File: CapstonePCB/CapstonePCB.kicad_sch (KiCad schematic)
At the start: 29 parts, among them J1 Conn_02x40_Counter_Clockwise, J2 Barrel_Jack, U1 NUCLEO64-F411RE, U2 LP-MSPM0G3507, U3 STSPIN220, U4 74HC14, U5 LM7805_TO220, U6 TLV1117-33, U8 APDS-9306

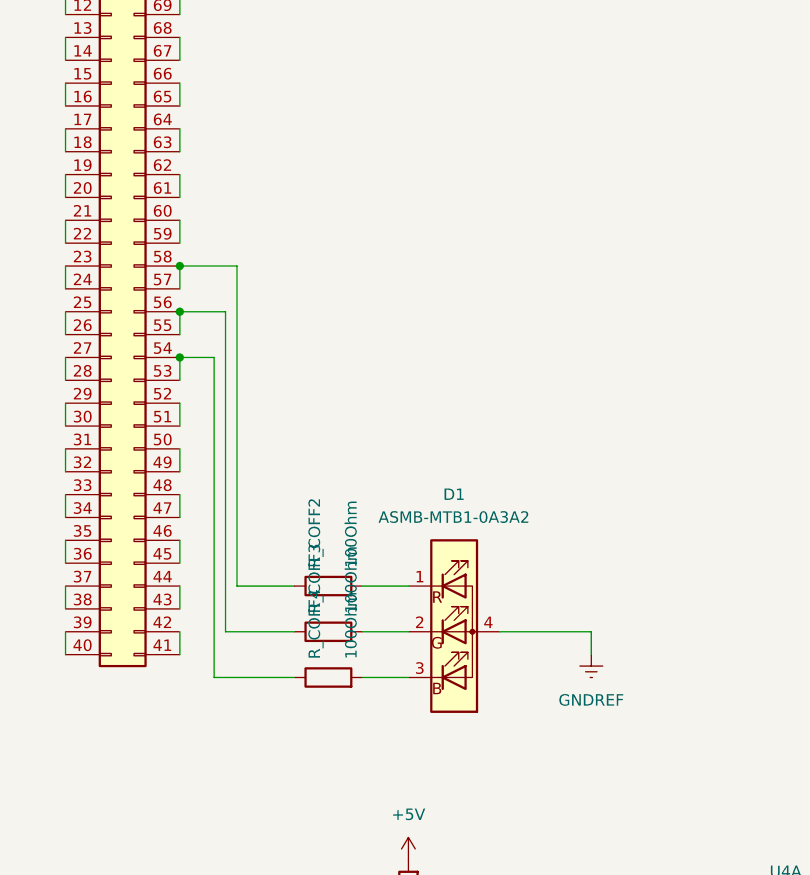
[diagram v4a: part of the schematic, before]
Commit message: Added footprints to motor driver circuit components
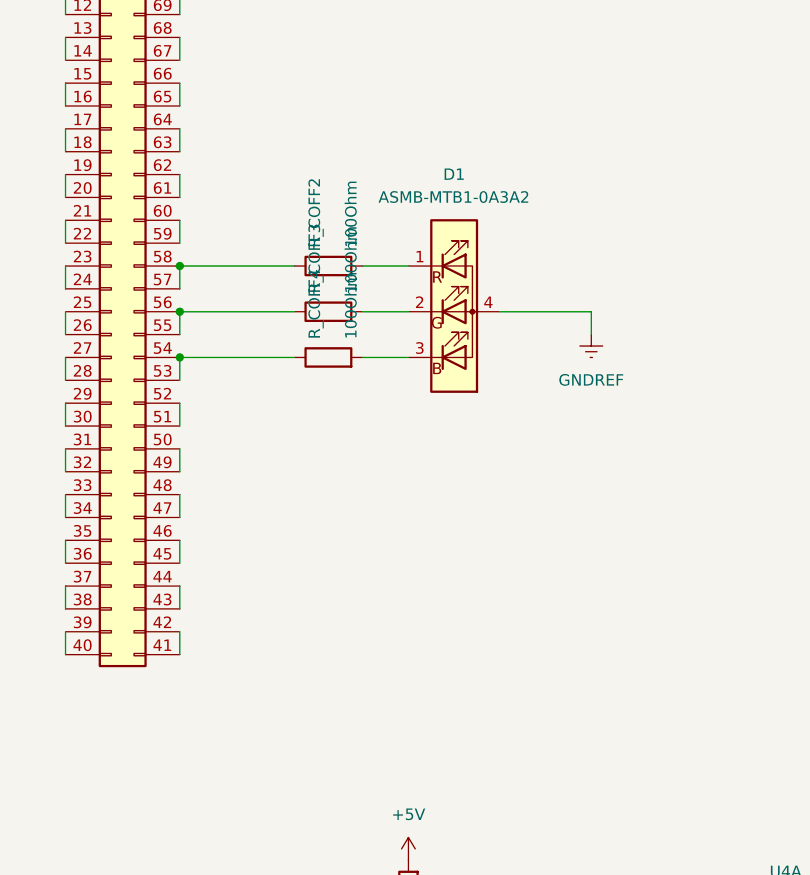
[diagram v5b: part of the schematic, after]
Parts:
- C_EN1, C_EN2, C_SPOIL1, C_STBY1, C_s1: footprint (none) -> Capacitor_SMD:C_0201_0603Metric
- R_COFF1, R_EN1, R_OFF1, R_SNSA1, R_SNSB1, R_STBY1: footprint (none) -> Resistor_SMD:R_0201_0603Metric
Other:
- moved on the sheet: D1, R_COFF2, R_COFF3, R_COFF4
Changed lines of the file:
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@@
 	(wire
 		(pts
-			(xy 160.02 115.57) (xy 152.4 115.57)
-		)
-		(stroke
-			(width 0)
-			(type default)
-		)
-	)
-	(wire
-		(pts
 			(xy 80.01 20.32) (xy 88.9 20.32)
 		)
@@
 	(wire
 		(pts
-			(xy 160.02 120.65) (xy 151.13 120.65)
-		)
-		(stroke
-			(width 0)
-			(type default)
-		)
-	)
-	(wire
-		(pts
 			(xy 134.62 85.09) (xy 134.62 87.63)
 		)
@@
 	(wire
 		(pts
-			(xy 193.04 115.57) (xy 193.04 118.11)
+			(xy 193.04 80.01) (xy 193.04 82.55)
 		)
 		(stroke
@@
 	(wire
 		(pts
-			(xy 153.67 110.49) (xy 153.67 74.93)
-		)
-		(stroke
-			(width 0)
-			(type default)
-		)
-	)
-	(wire
-		(pts
 			(xy 391.16 25.4) (xy 369.57 25.4)
 		)
@@
 	(wire
 		(pts
-			(xy 152.4 80.01) (xy 147.32 80.01)
+			(xy 147.32 80.01) (xy 160.02 80.01)
 		)
 		(stroke
@@
 	(wire
 		(pts
-			(xy 151.13 85.09) (xy 147.32 85.09)
+			(xy 147.32 85.09) (xy 160.02 85.09)
 		)
 		(stroke
@@
 	(wire
 		(pts
+			(xy 326.39 78.74) (xy 326.39 82.55)
+		)
+		(stroke
+			(width 0)
+			(type default)
+		)
+	)
+	(wire
+		(pts
 			(xy 318.77 50.8) (xy 318.77 53.34)
 		)
@@
 	(wire
 		(pts
-			(xy 167.64 110.49) (xy 172.72 110.49)
-		)
-		(stroke
-			(width 0)
-			(type default)
-		)
-	)
-	(wire
-		(pts
-			(xy 151.13 120.65) (xy 151.13 85.09)
+			(xy 167.64 74.93) (xy 172.72 74.93)
 		)
 		(stroke
@@
 	(wire
 		(pts
-			(xy 153.67 110.49) (xy 160.02 110.49)
-		)
-		(stroke
-			(width 0)
-			(type default)
-		)
-	)
-	(wire
-		(pts
 			(xy 104.14 20.32) (xy 107.95 20.32)
 		)
@@
 	(wire
 		(pts
-			(xy 152.4 115.57) (xy 152.4 80.01)
-		)
-		(stroke
-			(width 0)
-			(type default)
-		)
-	)
-	(wire
-		(pts
-			(xy 167.64 120.65) (xy 172.72 120.65)
+			(xy 167.64 85.09) (xy 172.72 85.09)
 		)
 		(stroke
@@
 	(wire
 		(pts
-			(xy 153.67 74.93) (xy 147.32 74.93)
+			(xy 147.32 74.93) (xy 160.02 74.93)
 		)
 		(stroke
@@
 	(wire
 		(pts
-			(xy 326.39 78.74) (xy 326.39 82.55)
-		)
-		(stroke
-			(width 0)
-			(type default)
-		)
-	)
-	(wire
-		(pts
 			(xy 134.62 39.37) (xy 134.62 41.91)
 		)
@@
 	(wire
 		(pts
-			(xy 182.88 115.57) (xy 193.04 115.57)
+			(xy 182.88 80.01) (xy 193.04 80.01)
 		)
 		(stroke
@@
 	(wire
 		(pts
-			(xy 167.64 115.57) (xy 172.72 115.57)
+			(xy 167.64 80.01) (xy 172.72 80.01)
 		)
 		(stroke
@@
 			)
 		)
-		(property "Footprint" ""
+		(property "Footprint" "Capacitor_SMD:C_0201_0603Metric"
 			(at 391.16 29.21 0)
 			(effects
@@
 	(symbol
 		(lib_id "Device:R")
-		(at 163.83 115.57 90)
+		(at 163.83 80.01 90)
 		(unit 1)
 		(exclude_from_sim no)
@@
 		(dnp no)
 		(property "Reference" "R_COFF3"
-			(at 162.306 113.538 0)
+			(at 162.306 77.978 0)
 			(effects
 				(font
@@
 		)
 		(property "Value" "100Ohm"
-			(at 166.37 113.538 0)
+			(at 166.37 77.978 0)
 			(effects
 				(font
@@
 		)
 		(property "Footprint" "Resistor_SMD:R_0201_0603Metric"
-			(at 163.83 117.348 90)
+			(at 163.83 81.788 90)
 			(effects
 				(font
@@
 		)
 		(property "Datasheet" "~"
-			(at 163.83 115.57 0)
+			(at 163.83 80.01 0)
 			(effects
 				(font
@@
 		)
 		(property "Description" "Resistor"
-			(at 163.83 115.57 0)
+			(at 163.83 80.01 0)
 			(effects
 				(font
@@
 			)
 		)
-		(property "Footprint" ""
+		(property "Footprint" "Resistor_SMD:R_0201_0603Metric"
 			(at 316.992 46.99 90)
 			(effects
@@
 			)
 		)
-		(property "Footprint" ""
+		(property "Footprint" "Capacitor_SMD:C_0201_0603Metric"
 			(at 326.39 85.09 0)
 			(effects
@@
 	(symbol
 		(lib_id "Device:R")
-		(at 163.83 110.49 90)
+		(at 163.83 74.93 90)
 		(unit 1)
 		(exclude_from_sim no)
@@
 		(dnp no)
 		(property "Reference" "R_COFF2"
-			(at 162.306 108.458 0)
+			(at 162.306 72.898 0)
 			(effects
 				(font
@@
 		)
 		(property "Value" "100Ohm"
-			(at 166.37 108.458 0)
+			(at 166.37 72.898 0)
 			(effects
 				(font
@@
 		)
 		(property "Footprint" "Resistor_SMD:R_0201_0603Metric"
-			(at 163.83 112.268 90)
+			(at 163.83 76.708 90)
 			(effects
 				(font
@@
 		)
 		(property "Datasheet" "~"
-			(at 163.83 110.49 0)
+			(at 163.83 74.93 0)
 			(effects
 				(font
@@
 		)
 		(property "Description" "Resistor"
-			(at 163.83 110.49 0)
+			(at 163.83 74.93 0)
 			(effects
 				(font
@@
 			)
 		)
-		(property "Footprint" ""
+		(property "Footprint" "Capacitor_SMD:C_0201_0603Metric"
 			(at 318.77 60.96 0)
 			(effects
@@
 	(symbol
 		(lib_id "power:GNDREF")
-		(at 193.04 118.11 0)
+		(at 193.04 82.55 0)
 		(unit 1)
 		(exclude_from_sim no)
@@
 		(fields_autoplaced yes)
 		(property "Reference" "#PWR023"
-			(at 193.04 124.46 0)
+			(at 193.04 88.9 0)
 			(effects
 				(font
@@
 		)
 		(property "Value" "GNDREF"
-			(at 193.04 123.19 0)
+			(at 193.04 87.63 0)
 			(effects
 				(font
@@
 		)
 		(property "Footprint" ""
-			(at 193.04 118.11 0)
+			(at 193.04 82.55 0)
 			(effects
 				(font
@@
 		)
 		(property "Datasheet" ""
-			(at 193.04 118.11 0)
+			(at 193.04 82.55 0)
 			(effects
 				(font
@@
 		)
 		(property "Description" ""
-			(at 193.04 118.11 0)
+			(at 193.04 82.55 0)
 			(effects
 				(font
@@
 			)
 		)
-		(property "Footprint" ""
+		(property "Footprint" "Resistor_SMD:R_0201_0603Metric"
 			(at 334.772 74.93 90)
 			(effects
@@
 			)
 		)
-		(property "Footprint" ""
+		(property "Footprint" "Resistor_SMD:R_0201_0603Metric"
 			(at 365.252 60.96 90)
 			(effects
@@
 			)
 		)
-		(property "Footprint" ""
+		(property "Footprint" "Resistor_SMD:R_0201_0603Metric"
 			(at 301.752 48.26 90)
 			(effects
@@
 			)
 		)
-		(property "Footprint" ""
+		(property "Footprint" "Resistor_SMD:R_0201_0603Metric"
 			(at 324.612 74.93 90)
 			(effects
@@
 			)
 		)
-		(property "Footprint" ""
+		(property "Footprint" "Capacitor_SMD:C_0201_0603Metric"
 			(at 369.57 29.21 0)
 			(effects
@@
 			)
 		)
-		(property "Footprint" ""
+		(property "Footprint" "Capacitor_SMD:C_0201_0603Metric"
 			(at 303.53 58.42 0)
 			(effects
@@
 			)
 		)
-		(property "Footprint" ""
+		(property "Footprint" "Resistor_SMD:R_0201_0603Metric"
 			(at 369.062 48.26 90)
 			(effects
@@
 	(symbol
 		(lib_id "LED:ASMB-MTB1-0A3A2")
-		(at 177.8 115.57 0)
+		(at 177.8 80.01 0)
 		(unit 1)
 		(exclude_from_sim no)
@@
 		(fields_autoplaced yes)
 		(property "Reference" "D1"
-			(at 177.8 100.33 0)
+			(at 177.8 64.77 0)
 			(effects
 				(font
@@
 		)
 		(property "Value" "ASMB-MTB1-0A3A2"
-			(at 177.8 102.87 0)
+			(at 177.8 67.31 0)
 			(effects
 				(font
@@
 		)
 		(property "Footprint" "LED_SMD:LED_Avago_PLCC4_3.2x2.8mm_CW"
-			(at 177.8 100.33 0)
+			(at 177.8 64.77 0)
 			(effects
 				(font
@@
 		)
 		(property "Datasheet" "https://docs.broadcom.com/docs/AV02-4194EN"
-			(at 177.8 127 0)
+			(at 177.8 91.44 0)
 			(effects
 				(font
@@
 		)
 		(property "Description" "Tricolor Black Surface LED, Common Anode Pin 4, PLCC-4"
-			(at 177.8 115.57 0)
+			(at 177.8 80.01 0)
 			(effects
 				(font
@@
 	(symbol
 		(lib_id "Device:R")
-		(at 163.83 120.65 90)
+		(at 163.83 85.09 90)
 		(unit 1)
 		(exclude_from_sim no)
@@
 		(dnp no)
 		(property "Reference" "R_COFF4"
-			(at 162.306 118.618 0)
+			(at 162.306 83.058 0)
 			(effects
 				(font
@@
 		)
 		(property "Value" "100Ohm"
-			(at 166.37 118.618 0)
+			(at 166.37 83.058 0)
 			(effects
 				(font
@@
 		)
 		(property "Footprint" "Resistor_SMD:R_0201_0603Metric"
-			(at 163.83 122.428 90)
+			(at 163.83 86.868 90)
 			(effects
 				(font
@@
 		)
 		(property "Datasheet" "~"
-			(at 163.83 120.65 0)
+			(at 163.83 85.09 0)
 			(effects
 				(font
@@
 		)
 		(property "Description" "Resistor"
-			(at 163.83 120.65 0)
+			(at 163.83 85.09 0)
 			(effects
 				(font

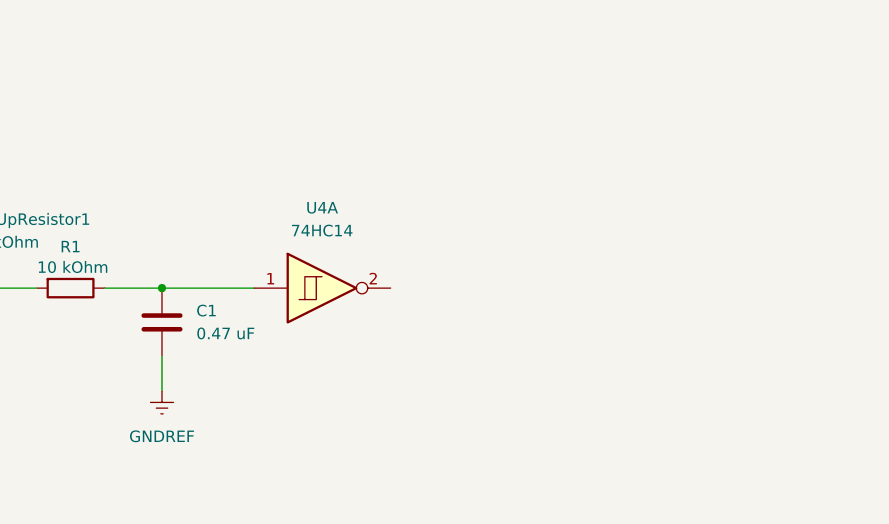
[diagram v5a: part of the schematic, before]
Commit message: Added in component for 8 bit schmitt trigger for button debouncing
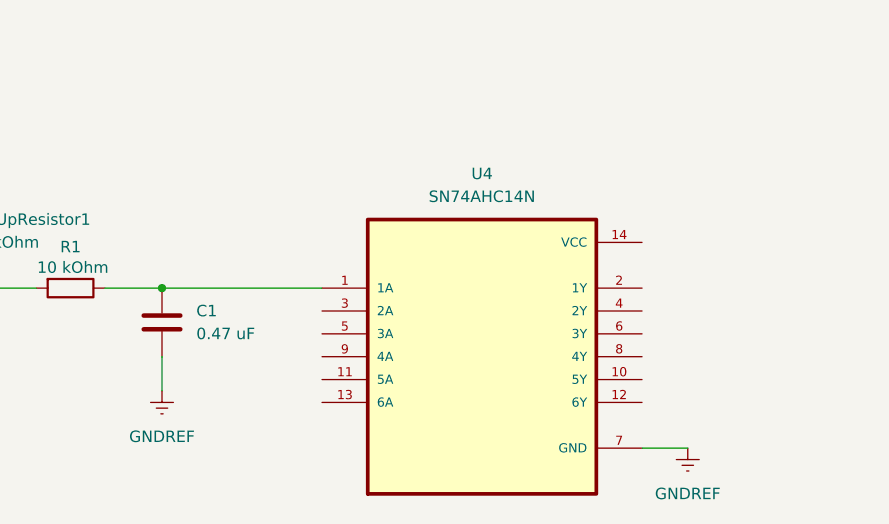
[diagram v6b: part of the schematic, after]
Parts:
- removed U4: 74HC14, symbol 74xx:74HC14
- added U4: SN74AHC14N, Schmitt:DIP794W45P254L1969H508Q14, symbol SN74AHC14N:SN74AHC14N
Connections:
- net GNDREF: now also U4.7 (GND)
- net at C1.1, R1.1: now also U4.1 (1A)

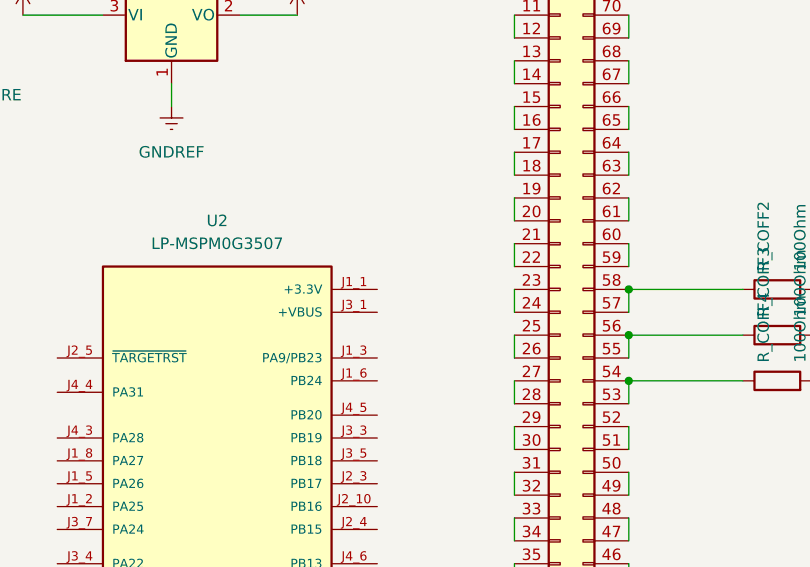
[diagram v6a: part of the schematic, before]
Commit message: Added power connection for mspm0 microcontroller
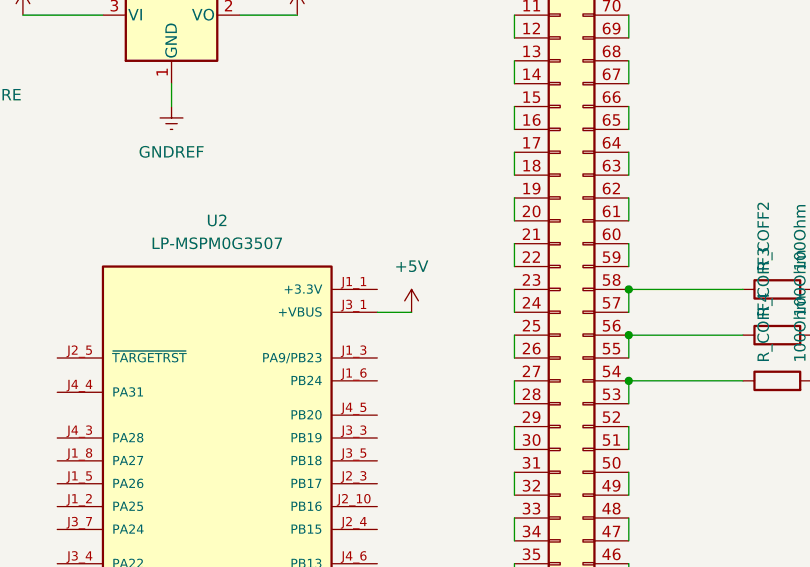
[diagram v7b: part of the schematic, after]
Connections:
- net +5V: now also U2.J3_1 (+VBUS)
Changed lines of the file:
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@@
+	(wire
+		(pts
+			(xy 119.38 77.47) (xy 123.19 77.47)
+		)
+		(stroke
+			(width 0)
+			(type default)
+		)
+	)
 	(wire
 		(pts
@@
 					(unit 1)
 				)
+			)
+		)
+	)
+	(symbol
+		(lib_id "power:+5V")
+		(at 123.19 77.47 0)
+		(unit 1)
+		(exclude_from_sim no)
+		(in_bom yes)
+		(on_board yes)
+		(dnp no)
+		(fields_autoplaced yes)
+		(property "Reference" "#PWR029"
+			(at 123.19 81.28 0)
+			(effects
+				(font
+					(size 1.27 1.27)
+				)
+				(hide yes)
+			)
+		)
+		(property "Value" "+5V"
+			(at 123.19 72.39 0)
+			(effects
+				(font
+					(size 1.27 1.27)
+				)
+			)
+		)
+		(property "Footprint" ""
+			(at 123.19 77.47 0)
+			(effects
+				(font
+					(size 1.27 1.27)
+				)
+				(hide yes)
+			)
+		)
+		(property "Datasheet" ""
+			(at 123.19 77.47 0)
+			(effects
+				(font
+					(size 1.27 1.27)
+				)
+				(hide yes)
+			)
+		)
+		(property "Description" "Power symbol creates a global label with name \"+5V\""
+			(at 123.19 77.47 0)
+			(effects
+				(font
+					(size 1.27 1.27)
+				)
+				(hide yes)
+			)
+		)
+		(pin "1"
+		)
+		(instances
+			(project "CapstonePCB"
+				(path "/39e7582f-7765-4fc9-b934-76d5b28d9065"
+					(reference "#PWR029")
+					(unit 1)
+				)
